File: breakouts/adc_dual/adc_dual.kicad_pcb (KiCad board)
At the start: 4 copper layers, 81 parts, among them P101 CONN_02X04, P102 CONN_01X02, P103 CONN_01X02, P104 CONN_01X02, P105 CONN_01X08, P106 CONN_01X08, P107 CONN_01X02, P108 CONN_01X02, U101 CONN_SMA, U102 CONN_SMA, U103 CONN_SMA, U104 LT1819, U105 LT1819, U106 TPS793, U107 LTC2323, U108 NC7SVU04, U109 NC7SVU04, U110 NC7SVU04, U111 NC7SVU04, U112 NC7SVU04, U113 NC7SV74KBX

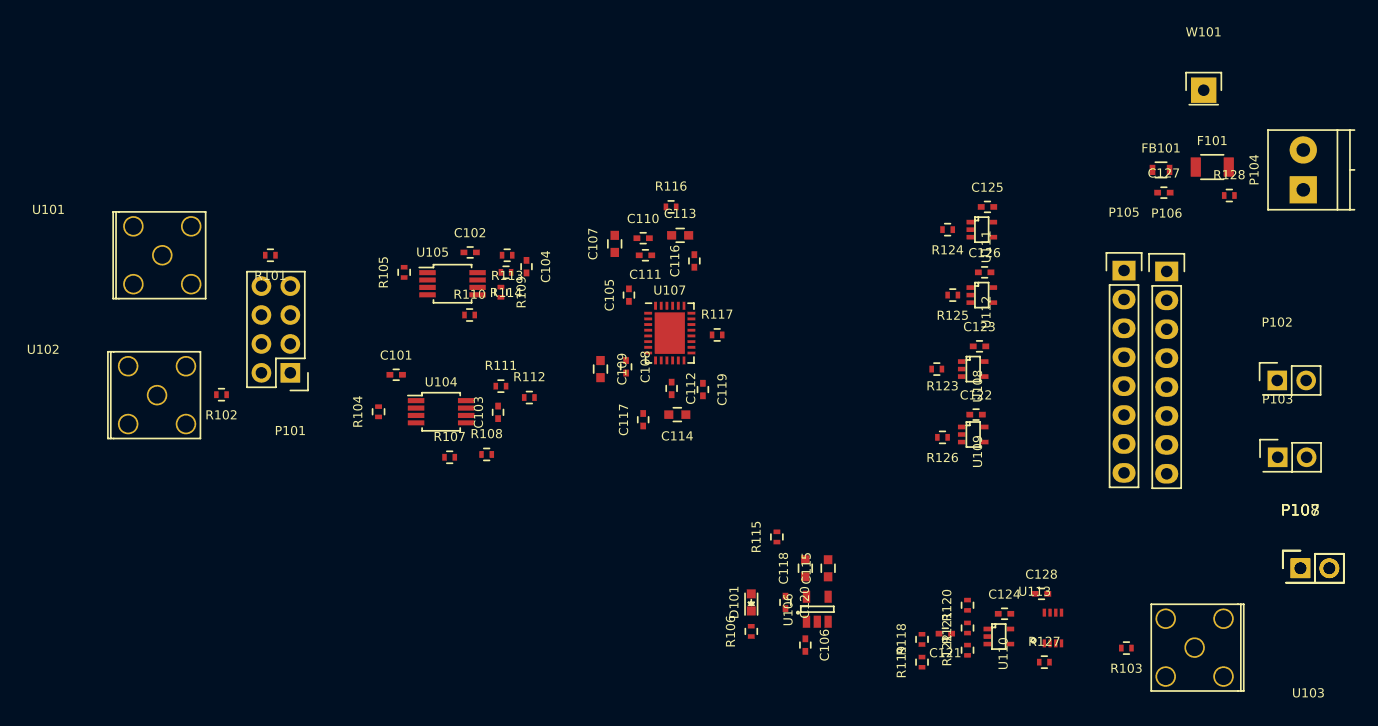
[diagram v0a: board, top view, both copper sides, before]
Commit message: layout of sections of the dual adc board
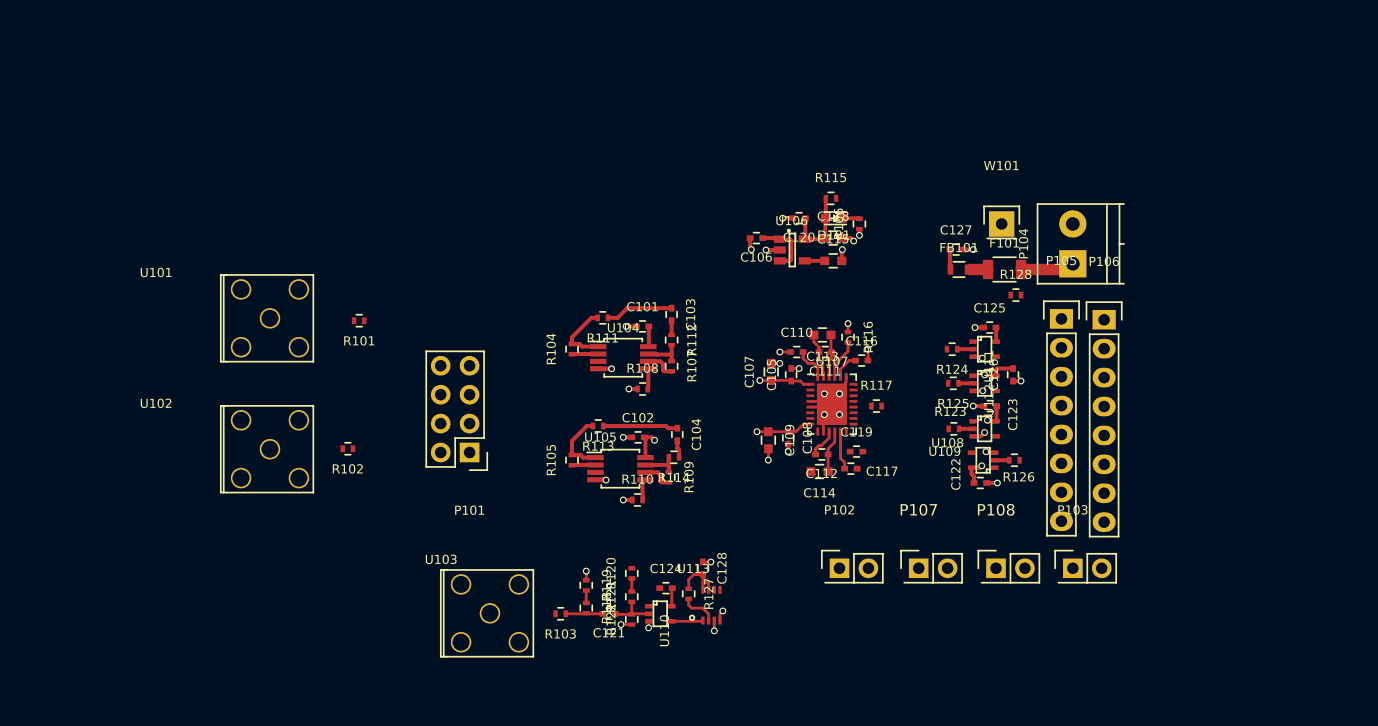
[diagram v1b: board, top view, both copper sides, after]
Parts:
- moved U103 62.0 mm to (202.8, 124.7), turned to 0 degrees
- moved R103 49.8 mm to (209.0, 124.8)
- moved P102 41.8 mm to (233.5, 120.8)
- moved R106 37.0 mm to (235.2, 90.5)
- moved C106 36.0 mm to (226.2, 91.7), turned to 180 degrees
- moved D101 34.5 mm to (233.0, 90.0), turned to 180 degrees
- moved C120 33.8 mm to (230.0, 90.0), turned to 180 degrees
- moved P107 33.5 mm to (240.5, 120.8)
- moved R127 31.8 mm to (220.2, 123.0), turned to 270 degrees
- moved U106 31.6 mm to (229.4, 92.8), turned to 0 degrees
- moved R119 30.3 mm to (211.2, 122.2), turned to 270 degrees
- moved R115 30.1 mm to (232.8, 88.2), turned to 0 degrees
- moved U113 30.1 mm to (222.2, 124.0)
- moved C124 29.8 mm to (218.2, 122.5)
- moved C128 29.8 mm to (221.5, 120.8), turned to 270 degrees
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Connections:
- U107 pad 9: (no net) -> /ADC_~CONV
- U113 pad 3: (no net) -> /ADC_~CONV
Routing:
- net GND: track 0.00 -> 39.0 mm, vias 0 -> 37
- net +5V: track 0.00 -> 24.2 mm, vias 0 -> 3
- net +2V5: track 0.00 -> 14.3 mm, vias 0 -> 1
- net /AIN1+: track 0.00 -> 6.58 mm
- net +3V3: track 0.00 -> 6.53 mm, vias 0 -> 2
- net /AIN2+: track 0.00 -> 5.95 mm
- net Net-(R104-Pad2): track 0.00 -> 5.95 mm
- net Net-(R105-Pad2): track 0.00 -> 5.81 mm
- net Net-(F101-Pad2): track 0.00 -> 4.76 mm
- net Net-(C111-Pad2): track 0.00 -> 4.46 mm
- net Net-(C121-Pad1): track 0.00 -> 4.08 mm
- net Net-(C111-Pad1): track 0.00 -> 3.83 mm
- net Net-(C112-Pad1): track 0.00 -> 3.76 mm
- net Net-(R116-Pad2): track 0.00 -> 3.52 mm
- net Net-(R107-Pad1): track 0.00 -> 3.48 mm
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
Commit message: adc layout complete (except for analog input traces..)
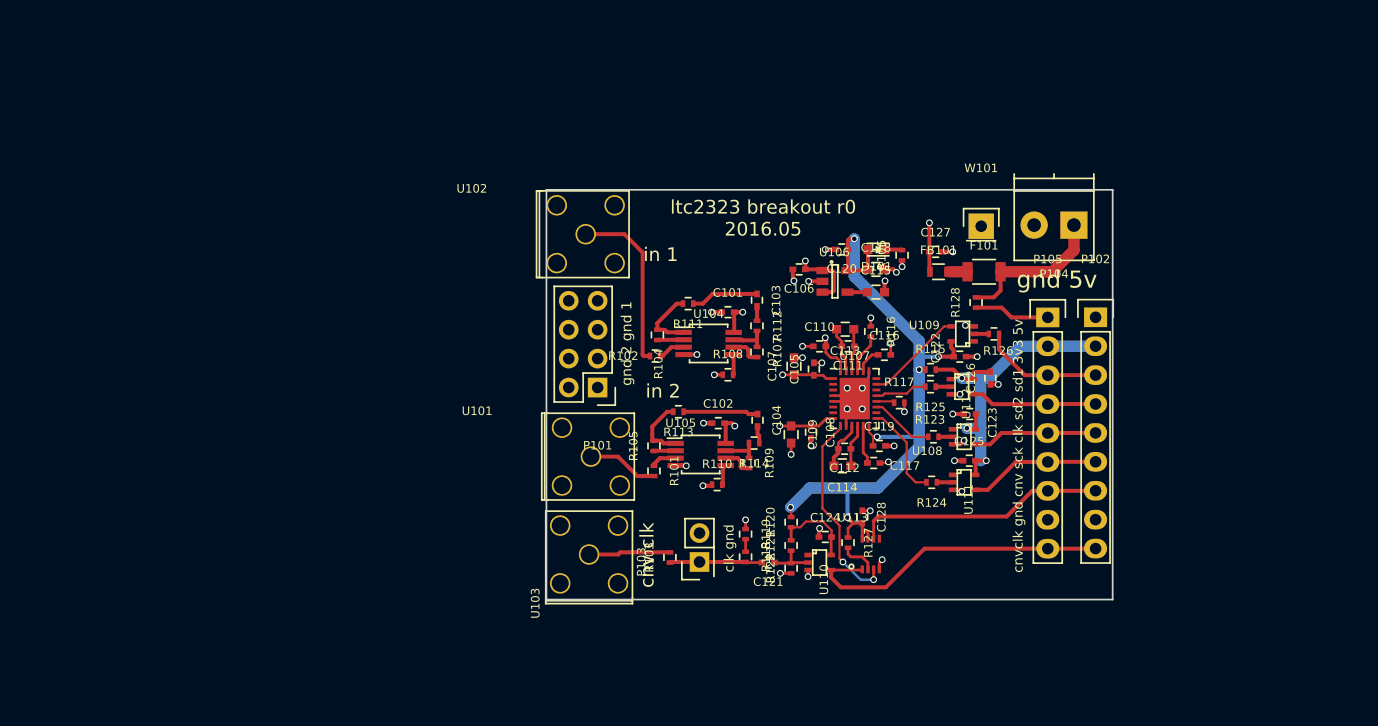
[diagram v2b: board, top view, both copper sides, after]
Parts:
- removed P106: CONN_01X08, Pin_Headers:Pin_Header_Straight_1x08
- removed P107, P108: CONN_01X02, Pin_Headers:Pin_Header_Straight_2x01
- P102: value CONN_01X02 -> CONN_01X09; footprint Pin_Headers:Pin_Header_Straight_2x01 -> Pin_Headers:Pin_Header_Straight_1x09
- P105: value CONN_01X08 -> CONN_01X09; footprint Pin_Headers:Pin_Header_Straight_1x08 -> Pin_Headers:Pin_Header_Straight_1x09
- moved U102 33.6 mm to (211.2, 91.4)
- moved P103 32.8 mm to (221.2, 120.2), turned to 90 degrees
- moved P102 31.5 mm to (256.0, 98.7)
- moved U101 30.7 mm to (211.7, 110.9)
- moved R101 29.1 mm to (217.2, 112.2), turned to 270 degrees
- moved R102 28.2 mm to (217.3, 102.1)
- moved R115 17.4 mm to (241.5, 103.3)
- moved C121 14.7 mm to (227.2, 120.2)
- moved C124 14.7 mm to (232.2, 118.0)
- moved C128 14.7 mm to (235.5, 116.2)
- moved R118 14.7 mm to (225.2, 119.8)
- moved R119 14.7 mm to (225.2, 117.8)
- moved R120 14.7 mm to (229.2, 116.7)
- moved R121 14.7 mm to (229.2, 118.8)
- moved R122 14.7 mm to (229.2, 120.8)
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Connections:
- P101 pad 3: /IN2_P -> /IN1_P
- P101 pad 4: /IN2_M -> /IN1_M
- P101 pad 7: /IN1_P -> /IN2_P
- P101 pad 8: /IN1_M -> /IN2_M
- P102 pad 1: /BUF_CONV_CLK -> Net-(P102-Pad1)
- P102 pad 2: GND -> +3V3
- P105 pad 1: Net-(P105-Pad1) -> Net-(P102-Pad1)
- P105 pad 3: /BUF_SDO1 -> /BUF_SCK
- P105 pad 6: /BUF_SCK -> /BUF_SDO1
- R128 pad 1: Net-(P105-Pad1) -> Net-(P102-Pad1)
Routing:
- net +2V5: track 14.3 -> 61.0 mm, vias 1 -> 6
- net /BUF_CONV_CLK: track 2.84 -> 28.5 mm
- net +3V3: track 6.53 -> 32.0 mm, vias 2 -> 3
- net /BUF_CONV: track 0.00 -> 22.2 mm
- net /ADC_~CONV: track 0.90 -> 17.6 mm, vias 1 -> 2
- net Net-(R102-Pad2): track 0.00 -> 15.4 mm
- net /BUF_SDO1: track 0.00 -> 11.6 mm
- net /BUF_SDO2: track 0.00 -> 11.1 mm
- net /BUF_CLKOUT: track 0.00 -> 10.9 mm
- net /BUF_SCK: track 0.00 -> 10.8 mm
- net Net-(F101-Pad2): track 4.76 -> 13.5 mm
- net /ADC_SCK: track 0.00 -> 8.68 mm
- net /ADC_SDO1: track 0.00 -> 8.32 mm
- net Net-(R103-Pad2): track 0.00 -> 7.18 mm
- net Net-(P102-Pad1): track 0.00 -> 6.66 mm
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- added copper zone on In2.Cu, net +5V
- added copper zone on In1.Cu, net GND
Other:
- board outline added: 49.8 x 36 mm
- net class Default: clearance 0.2 -> 0.13
- rule trace_clearance: 0.2 -> 0.13
- board text added: "clk gnd"
- board text added: "cnv clk"
- board text added: "cnvclk gnd cnv sck clk sd2 sd1 3v3 5v"
- board text added: "gnd 2 gnd 1"
- board text added: "gnd 5v"
- board text added: "in 1"
- board text added: "in 2"
- board text added: "ltc2323 breakout r0 2016.05"

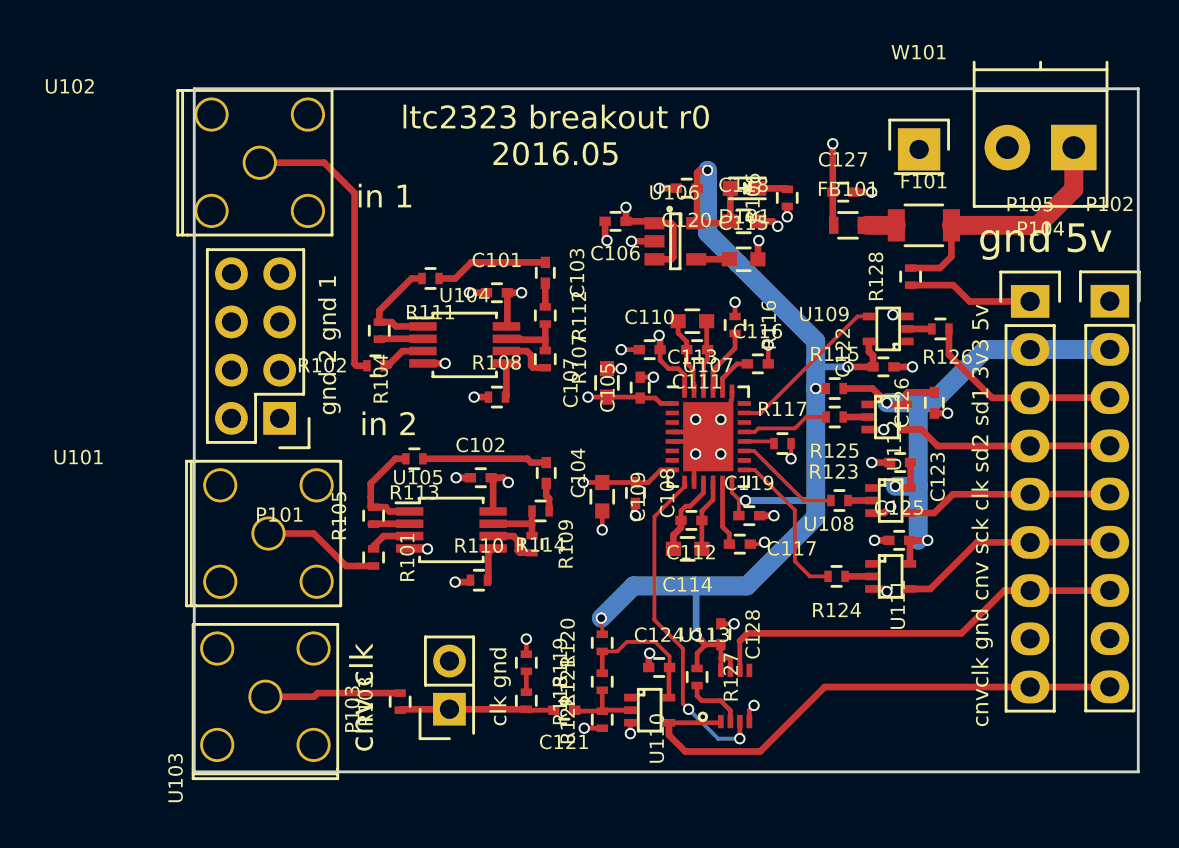
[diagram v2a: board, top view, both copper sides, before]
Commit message: finished adc layout
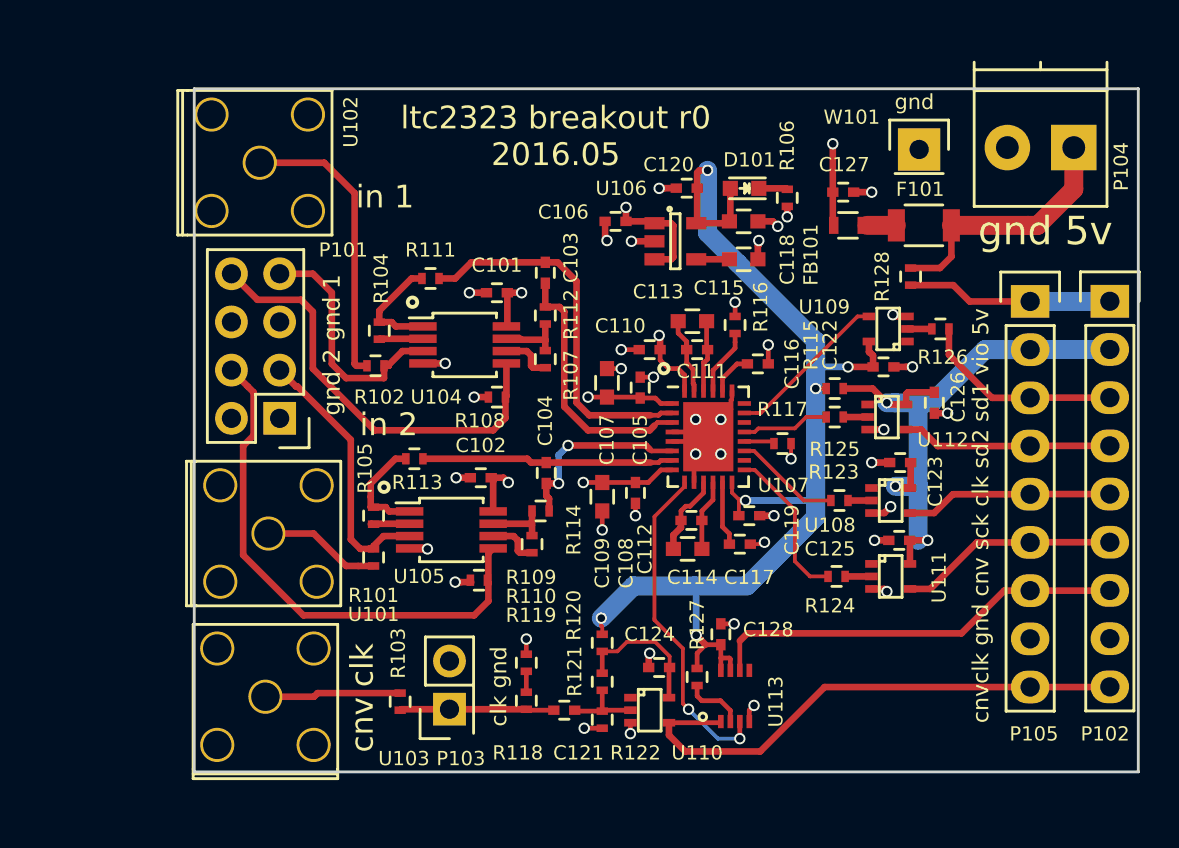
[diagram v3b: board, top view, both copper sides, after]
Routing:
- net /IN1_M: track 1.88 -> 28.0 mm
- net /IN2_M: track 1.80 -> 22.8 mm
- net /AIN2+: track 5.95 -> 19.8 mm
- net /AIN2-: track 1.25 -> 13.7 mm
- net /IN1_P: track 2.27 -> 14.2 mm
- net /IN2_P: track 2.40 -> 13.0 mm
- net /AIN1-: track 1.51 -> 9.98 mm, vias 0 -> 2
- net /AIN1+: track 6.58 -> 13.6 mm
- net Net-(P102-Pad1): track 6.66 -> 10.9 mm
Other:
- board text added: "cnvclk gnd cnv sck clk sd2 sd1 vio 5v"
- board text added: "gnd"
- board text removed: "cnvclk gnd cnv sck clk sd2 sd1 3v3 5v"
